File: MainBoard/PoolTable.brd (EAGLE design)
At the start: 457.2 x 166 mm, 26 parts, among them IC1 LM317MBSTT3, IC2 LM317MBSTT3, IC3 LM317MBSTT3, IC4 USB2517-JZX

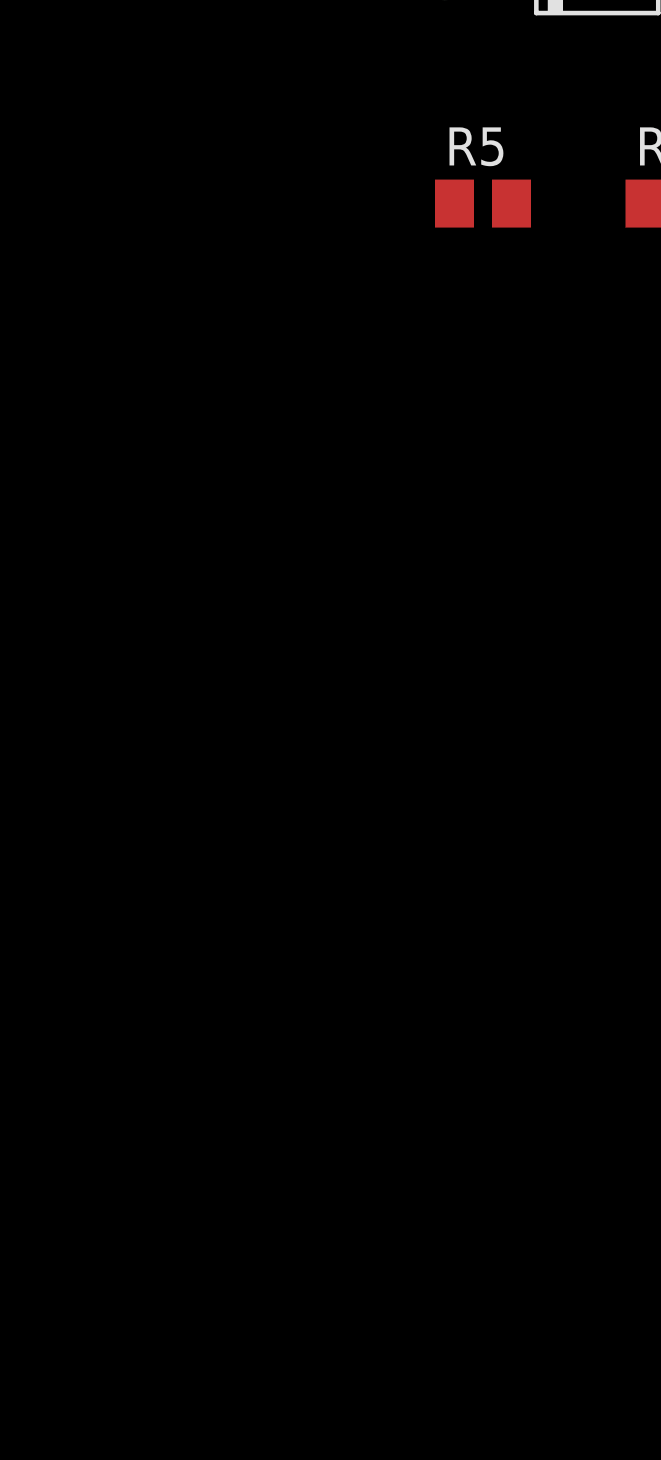
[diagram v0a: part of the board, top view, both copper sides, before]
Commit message: Added four temp sensors
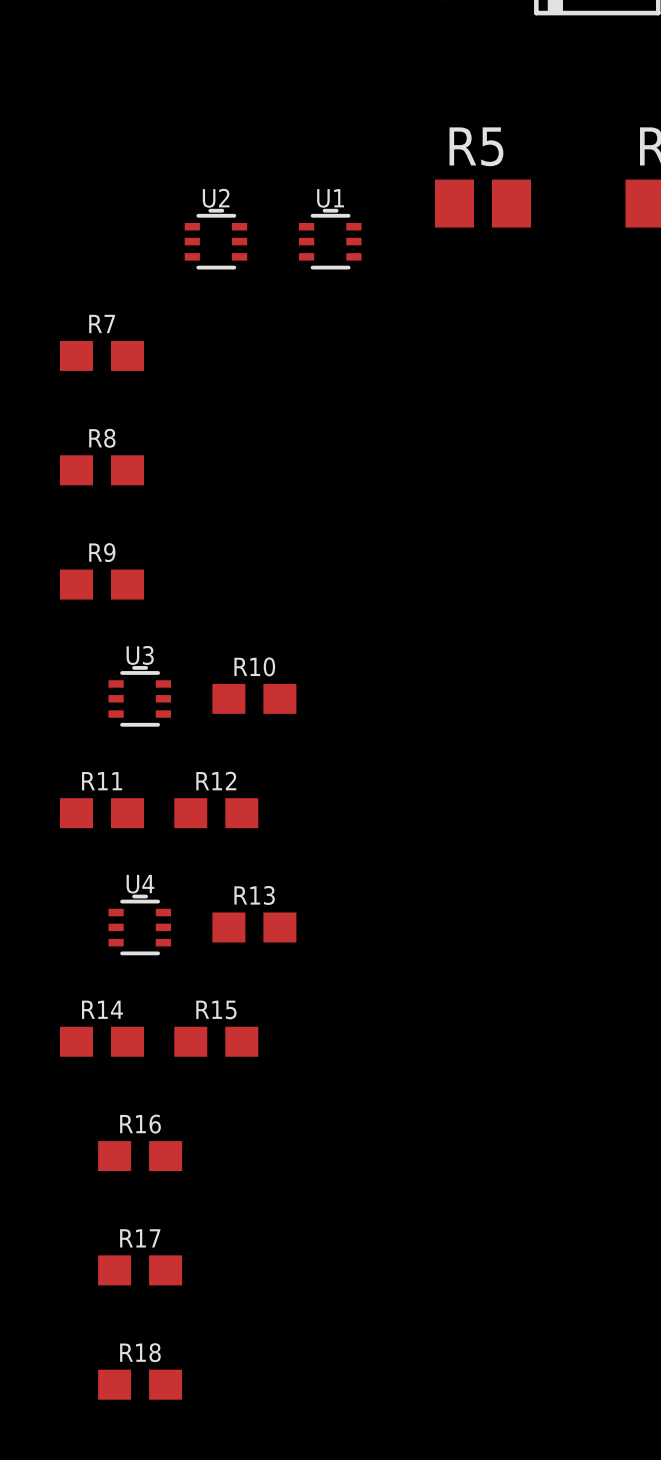
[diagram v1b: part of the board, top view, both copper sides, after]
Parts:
- added R10, R11, R12, R13, R14, R15, R16, R17, R18, R7, R8, R9: 5.6k, SparkFun-Resistors:0603
- added U1, U2, U3, U4: TMP102, SparkFun-Sensors:SOT563
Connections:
- new net N$10: R13.1, U4.6
- new net N$11: R14.1, U4.1, U4.4
- new net N$12: R15.1, U4.3
- new net N$13: R16.1, U2.6
- new net N$14: R17.1, U2.1
- new net N$15: R18.1, U2.3
- new net N$4: R7.1, U1.6
- new net N$5: R8.1, U1.1
- new net N$6: R9.1, U1.3
- new net N$7: R10.1, U3.4, U3.6
- new net N$8: R11.1, U3.1
- new net N$9: R12.1, U3.3
- net 3.3V: now also R10.2, R11.2, R12.2, R13.2, R14.2, R15.2, R16.2, R17.2, R18.2, R7.2, R8.2, R9.2, U1.5, U2.4, U2.5, U3.5, U4.5
- net GND: now also U1.2, U1.4, U2.2, U3.2, U4.2

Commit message: Started work on USB Hub/Ethernet
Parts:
- removed R16, R17: 5.6k, SparkFun-Resistors:0603
- added C10: 1.0uF, SparkFun-Capacitors:0402
- added D7, D8: GREEN, SparkFun-LED:LED-0603
- added IC5: MIC2026-1YM, micrel:SO08
- added J1, J2: USB_A_SMT_FEMALE, SparkFun-Connectors:USB-A-S-SILK-FEMALE
- added U$1, U$2, U$3: PWM_MODULE, Modules:PWM_MODULE
- added U$4, U$5: 47uF/6.3V, SparkFun-Capacitors:0805
- added U5: LAN9512-JZX, External:QFN64_9X9MC
- R10, R11, R7, R8: value 5.6k -> 4.7k
- R13, R14: value 5.6k -> 150
- moved R13 163.3 mm to (-43.2, -303.5)
- moved R14 162.1 mm to (-43.2, -307.3)
- moved R7 38.1 mm to (-8.89, -163.8)
- moved R8 38.1 mm to (-8.89, -167.6)
- moved R10 34.7 mm to (-10.2, -171.4)
- moved R11 34.3 mm to (-10.2, -175.3)
- moved C2 29.0 mm to (34.3, -10.2)
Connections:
- removed net N$13: R16.1, U2.6
- removed net N$14: R17.1, U2.1
- new net CPU1_ETH_PWR2: D8.A, IC5.8, J2.VBUS, U$4.1
- new net CPU1_ETH_PWR3: D7.A, IC5.5, J1.VBUS, U$5.1
- new net CPU1_ETH_VDD18CORE: U5.15, U5.38
- new net CPU1_ETH_VDD3A: U5.10, U5.49, U5.5, U5.51, U5.54, U5.57, U5.64
- new net N$16: D8.C, R13.2
- new net N$17: D7.C, R14.2
- new net PWM1_0: U$1.PWM0
- new net PWM1_1: U$1.PWM1
- new net PWM1_10: U$1.PWM10
- new net PWM1_11: U$1.PWM11
- new net PWM1_12: U$1.PWM12
- new net PWM1_13: U$1.PWM13
- new net PWM1_14: U$1.PWM14
- new net PWM1_15: U$1.PWM15
- new net PWM1_2: U$1.PWM2
- new net PWM1_3: U$1.PWM3
- new net PWM1_4: U$1.PWM4
- new net PWM1_5: U$1.PWM5
- new net PWM1_6: U$1.PWM6
- new net PWM1_7: U$1.PWM7
- new net PWM1_8: U$1.PWM8
- new net PWM1_9: U$1.PWM9
- new net PWM2_0: U$3.PWM0
- new net PWM2_1: U$3.PWM1
- new net PWM2_10: U$3.PWM10
- new net PWM2_11: U$3.PWM11
- new net PWM2_12: U$3.PWM12
- new net PWM2_13: U$3.PWM13
- new net PWM2_14: U$3.PWM14
- new net PWM2_15: U$3.PWM15
- new net PWM2_2: U$3.PWM2
- new net PWM2_3: U$3.PWM3
- new net PWM2_4: U$3.PWM4
- new net PWM2_5: U$3.PWM5
- new net PWM2_6: U$3.PWM6
- new net PWM2_7: U$3.PWM7
- new net PWM2_8: U$3.PWM8
- new net PWM2_9: U$3.PWM9
- new net PWM3_0: U$2.PWM0
- new net PWM3_1: U$2.PWM1
- new net PWM3_10: U$2.PWM10
- new net PWM3_11: U$2.PWM11
- new net PWM3_12: U$2.PWM12
- new net PWM3_13: U$2.PWM13
- new net PWM3_14: U$2.PWM14
- new net PWM3_15: U$2.PWM15
- new net PWM3_2: U$2.PWM2
- new net PWM3_3: U$2.PWM3
- new net PWM3_4: U$2.PWM4
- new net PWM3_5: U$2.PWM5
- new net PWM3_6: U$2.PWM6
- new net PWM3_7: U$2.PWM7
- new net PWM3_8: U$2.PWM8
- new net PWM3_9: U$2.PWM9
- new net VBUS_DET: U5.11
- new net VDD18ETHPLL: U5.48
- new net VDD18USBPLL: U5.62
- net 3.3V: now also U5.19, U5.27, U5.33, U5.39, U5.40, U5.46; no longer R10.2, R11.2, R13.2, R14.2, R16.2, R17.2, R7.2, R8.2
- net 5V: now also C10.2, IC5.7, R10.2, R11.2, R7.2, R8.2, U$1.5V, U$2.5V, U$3.5V
- net CPU1_SCL0: now also R7.1, U$1.SCL, U$2.SCL, U$3.SCL, U1.1, U2.1, U3.1, U4.1, U4.4
- net CPU1_SCL1: now also R10.1
- net CPU1_SDA0: now also R8.1, U$1.SDA, U$2.SDA, U$3.SDA, U1.6, U2.6, U3.4, U3.6, U4.6
- net CPU1_SDA1: now also R11.1
- net GND: now also C10.1, IC5.6, J1.GND, J1.SHLD1, J1.SHLD2, J2.GND, J2.SHLD1, J2.SHLD2, R13.1, R14.1, U$1.GND, U$2.GND, U$3.GND, U$4.2, U$5.2, U5.34, U5.65
- net N$10: now also IC5.1, IC5.2, U5.14; no longer R13.1, U4.6
- net N$11: now also IC5.3, IC5.4, U5.16; no longer R14.1, U4.1, U4.4
- net N$4: now also J2.D+, U5.2; no longer R7.1, U1.6
- net N$5: now also J2.D-, U5.1; no longer R8.1, U1.1
- net N$7: now also J1.D+, U5.4; no longer R10.1, U3.4, U3.6
- net N$8: now also J1.D-, U5.3; no longer R11.1, U3.1

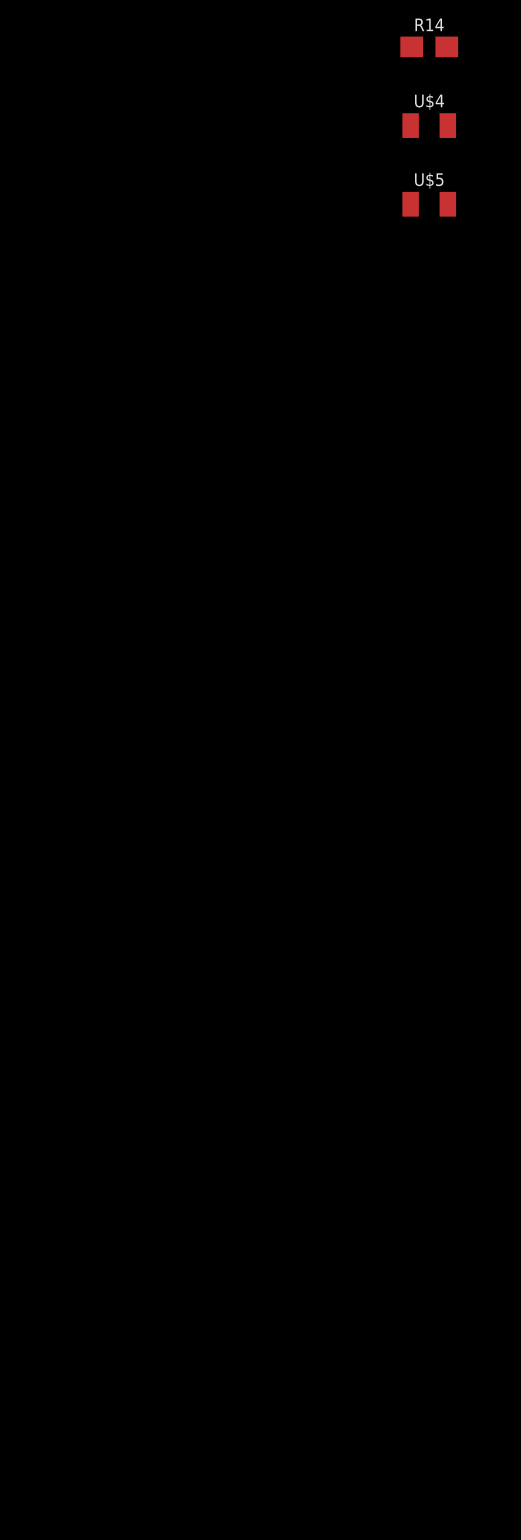
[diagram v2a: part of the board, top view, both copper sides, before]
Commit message: Implemented boot enable and finished USB
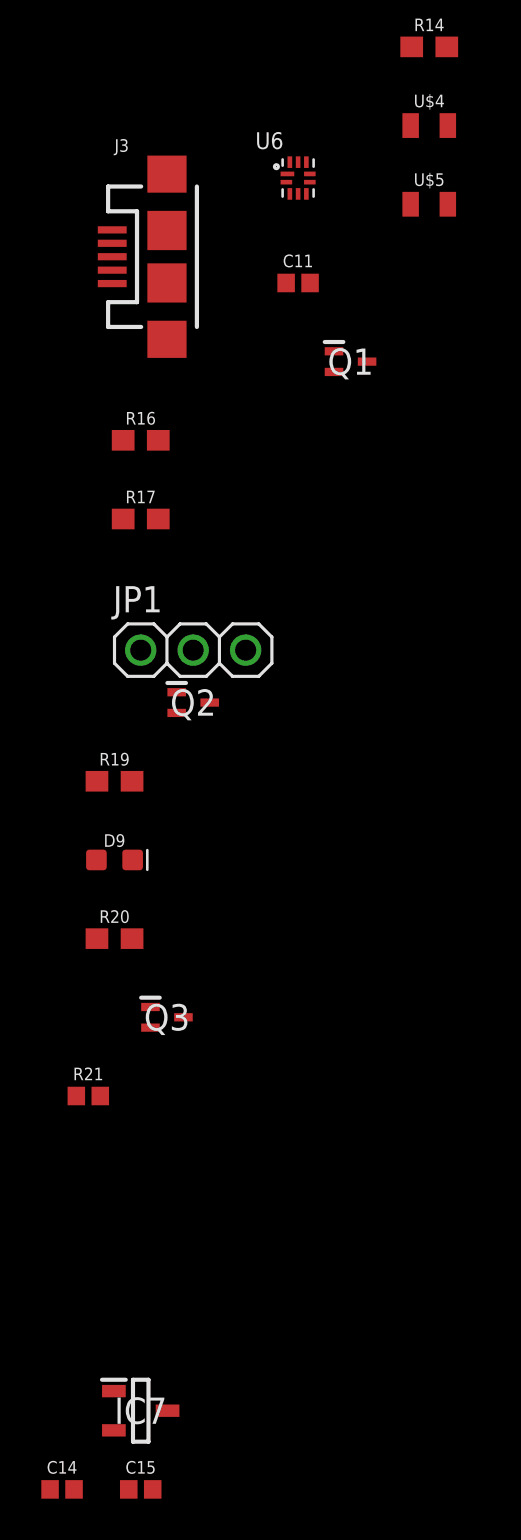
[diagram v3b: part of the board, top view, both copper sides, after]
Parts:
- added C11, C14, C15: 0.1uF, SparkFun-Capacitors:0402
- added D9: GREEN, SparkFun-LED:LED-0603
- added IC7: AP2331W-7, SamacSys_Parts:SOT95P285X130-3N
- added J3: (no value), SparkFun-Connectors:USB-MICROB
- added JP1: (no value), adafruit:1X03
- added Q1, Q2, Q3: DMG1012T-7, SamacSys_Parts:SOT50P160X80-3N
- added R16, R17, R19: 47k, SparkFun-Resistors:0603
- added R20: 150, SparkFun-Resistors:0603
- added R21: 100K, SparkFun-Resistors:0402
- added U6: FSUSB42UMX, FSUSB42UMX:IC_FSUSB42UMX
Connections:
- new net CPU1_EMMC_DISABLE_N: CPU1.2, Q2.3
- new net CPU1_EMMC_EN_N_1V8: CPU1.90, Q3.1, R21.2
- new net CPU1_ETH_USBDM: U5.58, U6.4
- new net CPU1_ETH_USBDP: U5.59, U6.5
- new net CPU1_VBUSB: J3.VBUS, JP1.1, Q1.1, R16.2
- new net H5V: C15.1, IC7.2
- new net N$13: CPU1.165, U6.1
- new net N$14: CPU1.167, U6.2
- new net N$18: J3.D+, U6.7
- new net N$19: Q1.2, R17.1, U6.10
- new net N$20: J3.D-, U6.6
- new net N$21: JP1.2, Q2.1, R19.2
- new net N$22: D9.C, Q2.2, Q3.3
- new net N$23: D9.A, R20.1
- net 1.8V: now also R21.1
- net 3.3V: now also C11.2, R17.2, R20.2, U6.9
- net 5V: now also C14.2, IC7.3
- net GND: now also C11.1, C14.1, C15.2, IC7.1, J3.GND, J3.MT1, J3.MT2, J3.P$1, J3.P$2, JP1.3, Q1.3, Q3.2, R16.1, R19.1, U6.3

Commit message: Cleaned up Schematic
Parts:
- removed IC4: USB2517-JZX, SamacSys_Parts:QFN50P900X900X100-65N
- added C12, C13: 4.7uF, SparkFun-Capacitors:0603
- added J4: SD_CARD_SOCKET, SparkFun-Connectors:SD
- added R22, R23, R24, R25: 100K, SparkFun-Resistors:0402
- added SJ1: (no value), jumper:SJ
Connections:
- net N$13 renamed CPU1_USB_D_P
- net N$14 renamed CPU1_USB_D_N
- removed net N$4: J2.D+, U5.2
- removed net N$5: J2.D-, U5.1
- removed net N$7: J1.D+, U5.4
- removed net N$8: J1.D-, U5.3
- removed net VDD18: IC4.25
- removed net VDD18PLL: IC4.62
- removed net VDD33: IC4.46
- removed net VDD33CR: IC4.24
- removed net VDD33PLL: IC4.64
- removed net VDDA33_1: IC4.5
- removed net VDDA33_2: IC4.10
- removed net VDDA33_3: IC4.52
- removed net VDDA33_4: IC4.57
- new net CPU1_ETH_USB_DM2: U5.1
- new net CPU1_ETH_USB_DM3: U5.3
- new net CPU1_ETH_USB_DP2: U5.2
- new net CPU1_ETH_USB_DP3: U5.4
- new net CPU1_SD_CLK: CPU1.10, J4.5
- new net CPU1_SD_CMD: CPU1.12, J4.2
- new net CPU1_SD_D0: CPU1.16, J4.7
- new net CPU1_SD_D1: CPU1.18, J4.8
- new net CPU1_SD_D2: CPU1.22, J4.9
- new net CPU1_SD_D3: CPU1.24, J4.1
- new net CPU1_SD_VREF: C13.2, CPU1.4, CPU1.6, SJ1.1
- net 3.3V: now also C12.1, J4.4, SJ1.2
- net CPU1_GPIO28: now also R22.1
- net CPU1_GPIO29: now also R23.1
- net CPU1_GPIO44: now also R24.1
- net CPU1_GPIO45: now also R25.1
- net GND: now also C12.2, C13.1, CPU1.14, CPU1.20, CPU1.8, J4.3, J4.6, J4.SH@1, J4.SH@2, R22.2, R23.2, R24.2, R25.2
